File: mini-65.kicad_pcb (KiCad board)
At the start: 2 copper layers, 308 x 98.4 mm, 167 parts, among them J1 AVR-ISP-6, J2 Conn_01x04, SW1 SW_Push, U1 ATmega32U4-AU, Y1 Crystal_GND24_Small

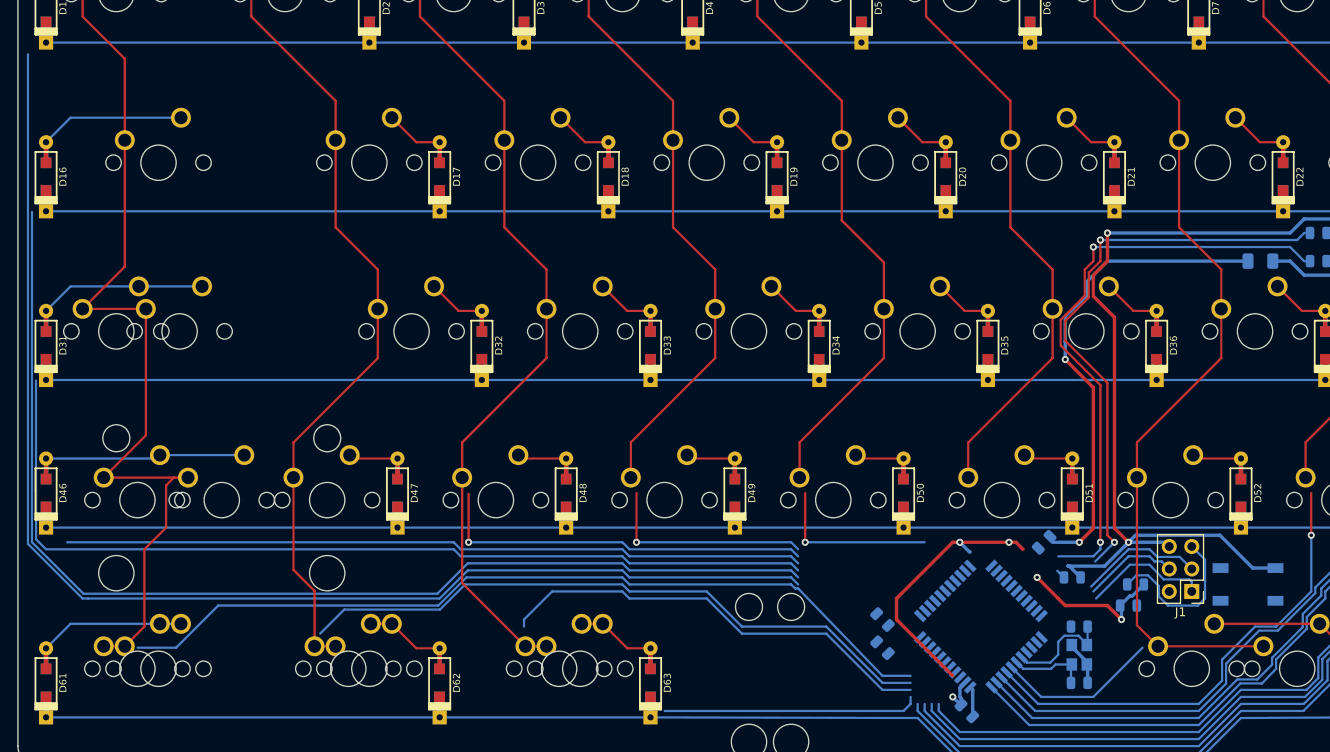
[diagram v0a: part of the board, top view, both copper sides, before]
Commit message: Routed the MCU and the components around it
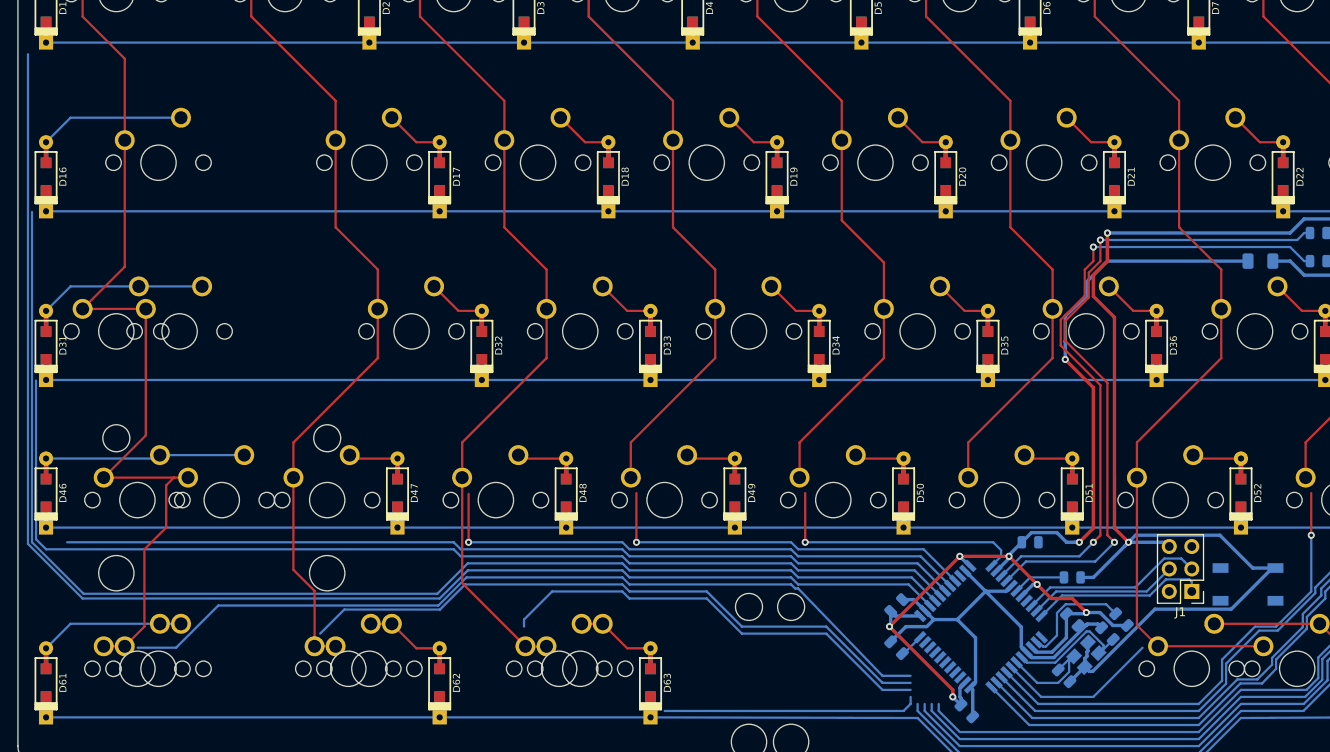
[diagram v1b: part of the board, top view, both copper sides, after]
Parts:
- moved C4 6.55 mm to (38.1, 159.5), turned to 315 degrees
- moved R1 4.27 mm to (43.7, 159.5), turned to 135 degrees
- moved C2 3.27 mm to (42.1, 161.1), turned to 135 degrees
- moved C6 2.25 mm to (18.3, 158.0), turned to 45 degrees
- moved C1 1.89 mm to (37.2, 165.9), turned to 315 degrees
- moved R4 1.59 mm to (18.3, 162.7)
- moved C7 1.59 mm to (33.3, 150.8), turned to 0 degrees
- moved Y1 0.79 mm to (39.7, 163.5), turned to 45 degrees
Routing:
- net GND: track 112.3 -> 189.4 mm
- net +5V: track 105.9 -> 131.0 mm, vias 7 -> 8
- net Net-(U1-Pad41): track 24.1 -> 43.4 mm
- net Net-(U1-Pad40): track 43.3 -> 61.9 mm
- net Net-(U1-Pad39): track 83.5 -> 101.4 mm
- net Net-(U1-Pad38): track 105.4 -> 122.7 mm
- net Net-(U1-Pad37): track 128.3 -> 144.9 mm
- net Net-(U1-Pad36): track 146.8 -> 162.7 mm
- net Net-(U1-Pad1): track 19.1 -> 30.3 mm
- net Net-(R2-Pad1): track 65.1 -> 76.1 mm
- net SCK: track 14.0 -> 20.8 mm
- net Net-(R3-Pad1): track 67.7 -> 74.1 mm
- net MOSI: track 10.8 -> 16.9 mm
- net MISO: track 14.3 -> 19.9 mm
- net RESET: track 18.1 -> 13.0 mm
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
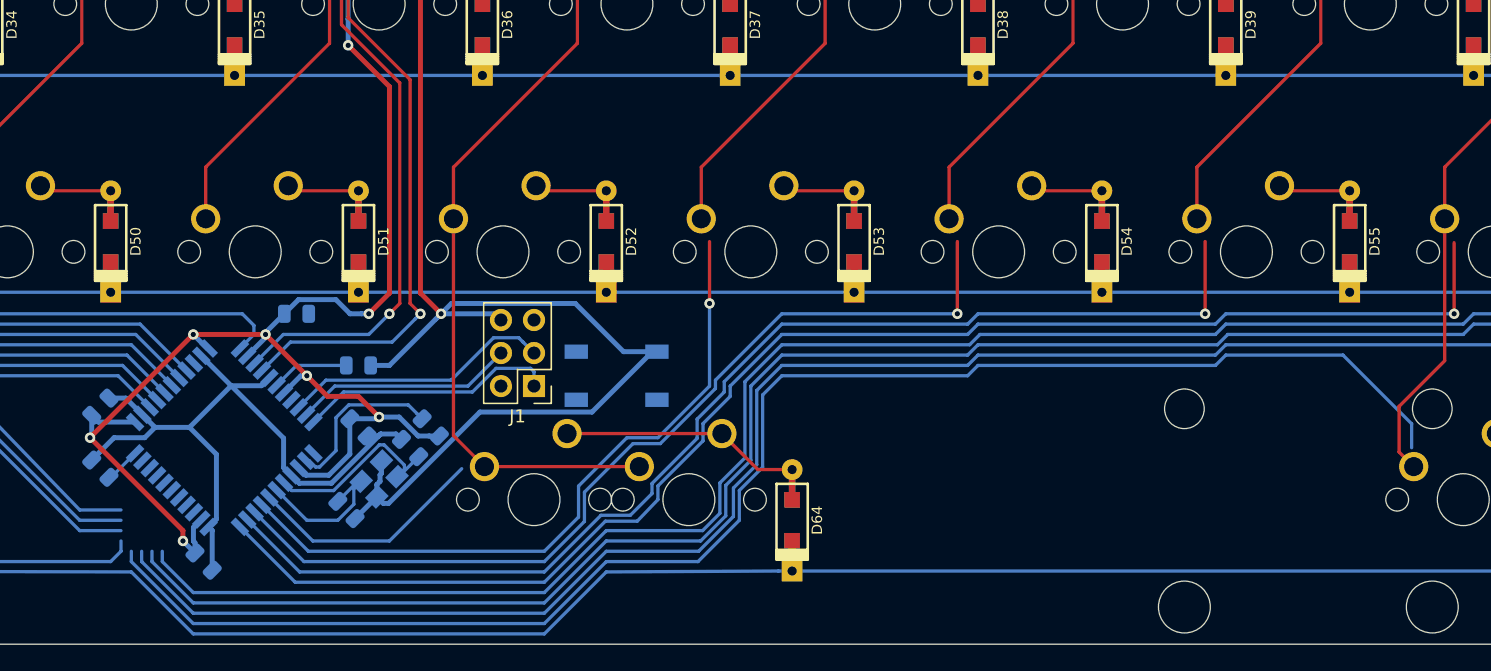
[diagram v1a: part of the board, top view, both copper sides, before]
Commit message: Mostly routed, FORGOT COL13
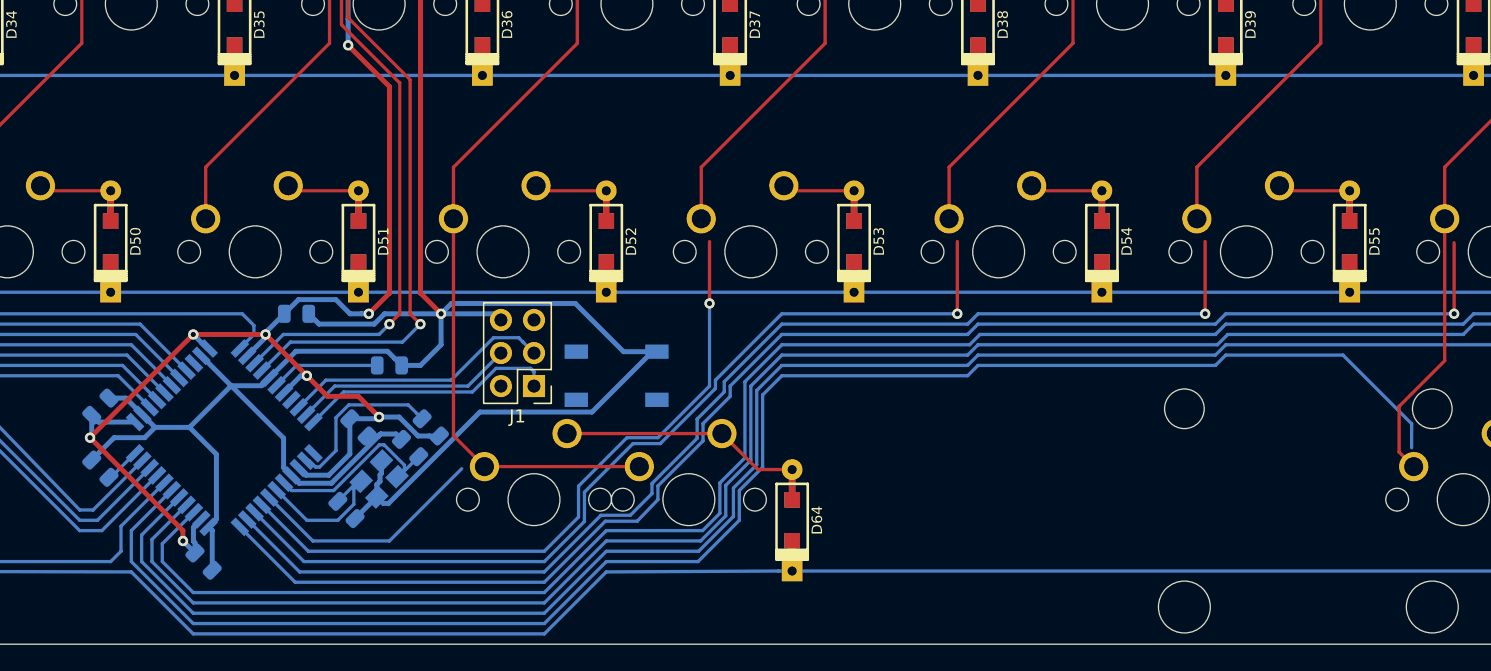
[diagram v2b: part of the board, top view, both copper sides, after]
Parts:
- moved C3 2.38 mm to (40.5, 154.8)
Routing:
- net GND: track 189.4 -> 210.7 mm
- net Net-(U1-Pad28): track 118.4 -> 124.4 mm
- net Net-(U1-Pad29): track 28.9 -> 34.8 mm
- net Net-(U1-Pad27): track 140.7 -> 146.1 mm
- net Net-(U1-Pad26): track 191.9 -> 196.6 mm
- net Net-(U1-Pad30): track 50.4 -> 54.9 mm
- net Net-(U1-Pad25): track 212.0 -> 216.0 mm
- net Net-(U1-Pad31): track 73.6 -> 77.5 mm
- net Net-(U1-Pad32): track 95.3 -> 98.5 mm
- net Net-(C3-Pad1): track 5.98 -> 8.36 mm

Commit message: Routed up all the cols/rows, properly this time
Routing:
- net Net-(U1-Pad27): track 146.1 -> 194.7 mm
- net Net-(U1-Pad28): track 124.4 -> 148.1 mm
- net RESET: track 13.0 -> 33.1 mm
- net Net-(U1-Pad1): track 30.3 -> 10.9 mm
- net Net-(U1-Pad41): track 43.4 -> 24.3 mm
- net Net-(U1-Pad40): track 61.9 -> 43.0 mm
- net Net-(U1-Pad26): track 196.6 -> 193.4 mm
- net Net-(U1-Pad30): track 54.9 -> 56.3 mm
- net Net-(U1-Pad32): track 98.5 -> 99.5 mm
- net Net-(U1-Pad39): track 101.4 -> 102.2 mm
- net Net-(U1-Pad36): track 162.7 -> 163.4 mm
- net Net-(U1-Pad37): track 144.9 -> 145.5 mm
- net Net-(U1-Pad31): track 77.5 -> 78.1 mm

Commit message: Routed most of the matrix
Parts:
- J1: moved to B.Cu
- moved C1 6.99 mm to (44.2, 165.9), turned to 90 degrees
- moved C2 6.39 mm to (37.8, 165.9), turned to 270 degrees
- moved C4 3.55 mm to (39.7, 162.7), turned to 180 degrees
- moved Y1 2.71 mm to (41.0, 165.9), turned to 180 degrees
- moved R1 2.38 mm to (43.7, 161.9), turned to 90 degrees
- moved J1 1.12 mm to (52.4, 157.2), turned to 90 degrees
- turned SW1 to 180 degrees
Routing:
- net Net-(U1-Pad22): track 111.0 -> 0.00 mm, vias 1 -> 0
- net Net-(U1-Pad21): track 90.9 -> 199.9 mm, vias 1 -> 0
- net Net-(U1-Pad27): track 194.7 -> 145.1 mm
- net Net-(U1-Pad18): track 18.5 -> 52.6 mm, vias 0 -> 1
- net Net-(U1-Pad25): track 216.0 -> 190.7 mm
- net Net-(U1-Pad28): track 148.1 -> 124.3 mm
- net GND: track 210.7 -> 190.6 mm
- net Net-(U1-Pad20): track 70.7 -> 90.1 mm
- net +5V: track 131.0 -> 148.5 mm
- net RESET: track 33.1 -> 49.7 mm
- net Net-(U1-Pad19): track 53.7 -> 69.9 mm
- net Net-(U1-Pad12): track 0.00 -> 13.7 mm
- net (no net): track 8.73 -> 0.00 mm
- net MOSI: track 16.9 -> 21.7 mm
- net Net-(C2-Pad1): track 15.0 -> 11.5 mm
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
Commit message: rerouted some of the lines
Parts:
- removed F2: 500mA, Fuse:Fuse_1206_3216Metric
- added F1: 500mA, Fuse:Fuse_1206_3216Metric, B.Cu at (59.5, 119.1)
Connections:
- U1 pad 1: Net-(U1-Pad1) -> COL5
- U1 pad 12: Net-(U1-Pad12) -> COL6
- U1 pad 18: Net-(U1-Pad18) -> COL7
- U1 pad 19: Net-(U1-Pad19) -> COL8
- U1 pad 20: Net-(U1-Pad20) -> COL9
- U1 pad 21: Net-(U1-Pad21) -> COL14
- U1 pad 25: Net-(U1-Pad25) -> COL13
- U1 pad 26: Net-(U1-Pad26) -> COL12
- U1 pad 27: Net-(U1-Pad27) -> COL11
- U1 pad 28: Net-(U1-Pad28) -> COL10
- U1 pad 29: Net-(U1-Pad29) -> ROW4
- U1 pad 30: Net-(U1-Pad30) -> COL2
- U1 pad 31: Net-(U1-Pad31) -> COL1
- U1 pad 32: Net-(U1-Pad32) -> COL0
- U1 pad 36: Net-(U1-Pad36) -> ROW0
- U1 pad 37: Net-(U1-Pad37) -> ROW1
- U1 pad 38: Net-(U1-Pad38) -> ROW2
- U1 pad 39: Net-(U1-Pad39) -> ROW3
- U1 pad 40: Net-(U1-Pad40) -> COL3
- U1 pad 41: Net-(U1-Pad41) -> COL4
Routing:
- net COL14: track 76.2 -> 276.1 mm
- net Net-(U1-Pad21): track 199.9 -> 0.00 mm
- net Net-(U1-Pad26): track 192.8 -> 0.00 mm
- net COL12: track 105.0 -> 297.8 mm
- net COL13: track 97.3 -> 288.0 mm
- net Net-(U1-Pad25): track 190.7 -> 0.00 mm
- net Net-(U1-Pad36): track 163.4 -> 0.00 mm
- net ROW0: track 301.6 -> 465.0 mm
- net ROW1: track 303.0 -> 448.6 mm
- net Net-(U1-Pad37): track 145.5 -> 0.00 mm
- net Net-(U1-Pad27): track 145.1 -> 0.00 mm
- net COL11: track 88.4 -> 233.6 mm
- net COL10: track 88.0 -> 212.3 mm
- net Net-(U1-Pad28): track 124.3 -> 0.00 mm
- net Net-(U1-Pad38): track 122.7 -> 0.00 mm
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
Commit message: before changing MCU position
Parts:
- moved F1 2.51 mm to (57.1, 119.9)
- moved R4 1.12 mm to (17.5, 161.9)
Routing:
- net COL10: track 212.3 -> 220.8 mm
- net COL14: track 276.1 -> 281.0 mm
- net +5V: track 148.5 -> 144.1 mm
- net COL12: track 297.8 -> 301.2 mm
- net COL11: track 233.6 -> 236.6 mm
- net ROW3: track 403.9 -> 406.7 mm
- net VCC: track 14.8 -> 17.3 mm
- net ROW0: track 465.0 -> 467.2 mm
- net COL8: track 136.9 -> 138.9 mm
- net COL5: track 77.9 -> 79.9 mm
- net COL3: track 110.0 -> 112.0 mm
- net COL4: track 91.3 -> 93.3 mm
- net Net-(R2-Pad1): track 76.5 -> 74.6 mm
- net COL9: track 157.1 -> 159.0 mm
- net ROW4: track 340.3 -> 342.1 mm
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
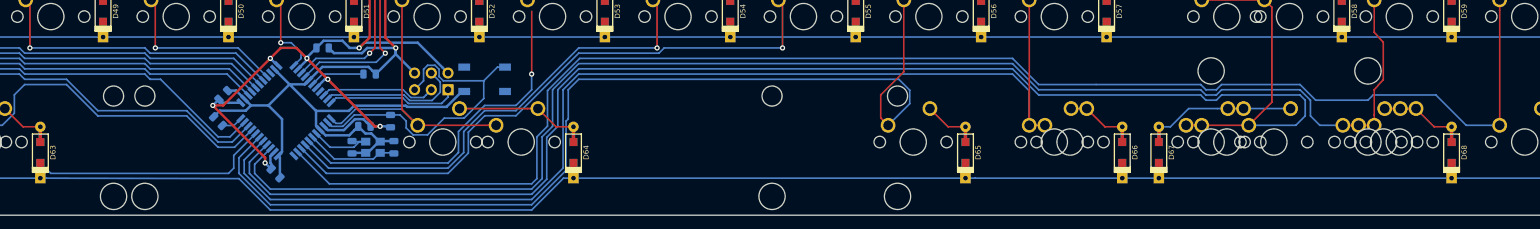
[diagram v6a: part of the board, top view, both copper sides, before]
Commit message: moved MCU left
havent attached all routes yet
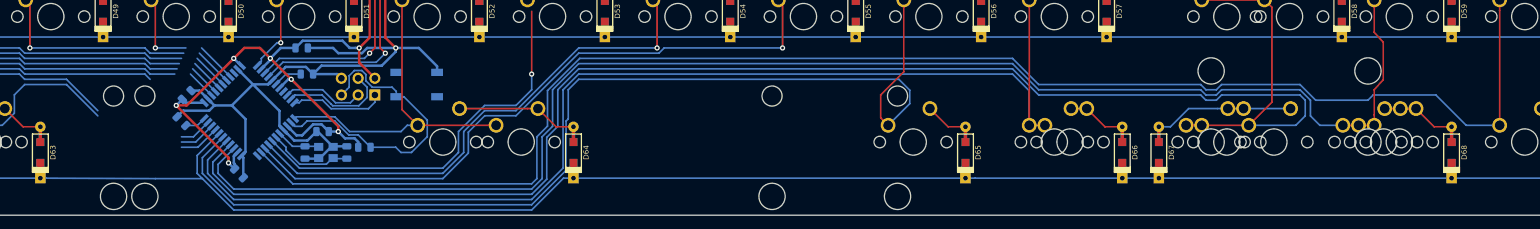
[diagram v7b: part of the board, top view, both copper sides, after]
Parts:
- moved J1 11.1 mm to (41.3, 158.0)
- moved SW1 10.3 mm to (47.6, 156.4), turned to 0 degrees
- moved C3 9.53 mm to (31.0, 154.8)
- moved C2 7.19 mm to (30.7, 166.7)
- moved C1 7.19 mm to (37.0, 166.7)
- moved Y1 7.19 mm to (33.8, 166.7)
- moved C4 6.40 mm to (33.3, 163.5)
- moved R1 5.61 mm to (39.7, 165.9), turned to 0 degrees
- moved C5 5.56 mm to (20.6, 169.9)
- moved C6 5.56 mm to (12.7, 158.0)
- moved R4 5.56 mm to (11.9, 161.9)
- moved U1 5.56 mm to (22.2, 160.3)
- moved C7 3.17 mm to (30.2, 150.8)
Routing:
- net ROW4: track 342.1 -> 314.2 mm
- net COL2: track 144.5 -> 124.3 mm
- net COL1: track 165.1 -> 144.8 mm
- net COL0: track 202.6 -> 188.7 mm
- net GND: track 191.1 -> 182.0 mm
- net ROW3: track 406.7 -> 398.8 mm
- net ROW2: track 424.8 -> 416.9 mm
- net ROW1: track 449.3 -> 441.4 mm
- net ROW0: track 467.2 -> 459.2 mm
- net COL3: track 112.0 -> 104.1 mm
- net COL4: track 93.3 -> 85.4 mm
- net COL8: track 138.9 -> 145.2 mm
- net COL9: track 159.0 -> 165.2 mm
- net COL7: track 120.6 -> 126.8 mm
- net COL13: track 289.2 -> 294.7 mm
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
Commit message: Step before USB Type C connector
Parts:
- moved C4 0.81 mm to (33.5, 162.7)
- moved R1 0.79 mm to (38.9, 165.9), turned to 270 degrees
- moved C1 0.79 mm to (37.0, 165.9)
- moved C2 0.79 mm to (30.7, 165.9)
- moved Y1 0.79 mm to (33.8, 165.9)
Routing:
- net COL2: track 124.3 -> 139.0 mm
- net COL1: track 144.8 -> 159.5 mm
- net COL0: track 188.7 -> 199.6 mm
- net RESET: track 46.5 -> 50.1 mm
- net ROW1: track 441.4 -> 443.8 mm
- net ROW3: track 398.8 -> 401.2 mm
- net ROW2: track 416.9 -> 419.3 mm
- net COL3: track 104.1 -> 106.5 mm
- net COL4: track 85.4 -> 87.8 mm
- net ROW0: track 459.2 -> 461.6 mm
- net +5V: track 142.1 -> 140.6 mm
- net MOSI: track 16.5 -> 17.2 mm
- net SCK: track 12.4 -> 13.1 mm
- net MISO: track 14.4 -> 15.1 mm
- net GND: track 182.0 -> 181.5 mm
